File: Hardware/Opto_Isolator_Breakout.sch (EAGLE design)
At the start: 16 parts, among them Q1 NPN, Q2 NPN, U1 OPTOISOLATOR-2SOIC8

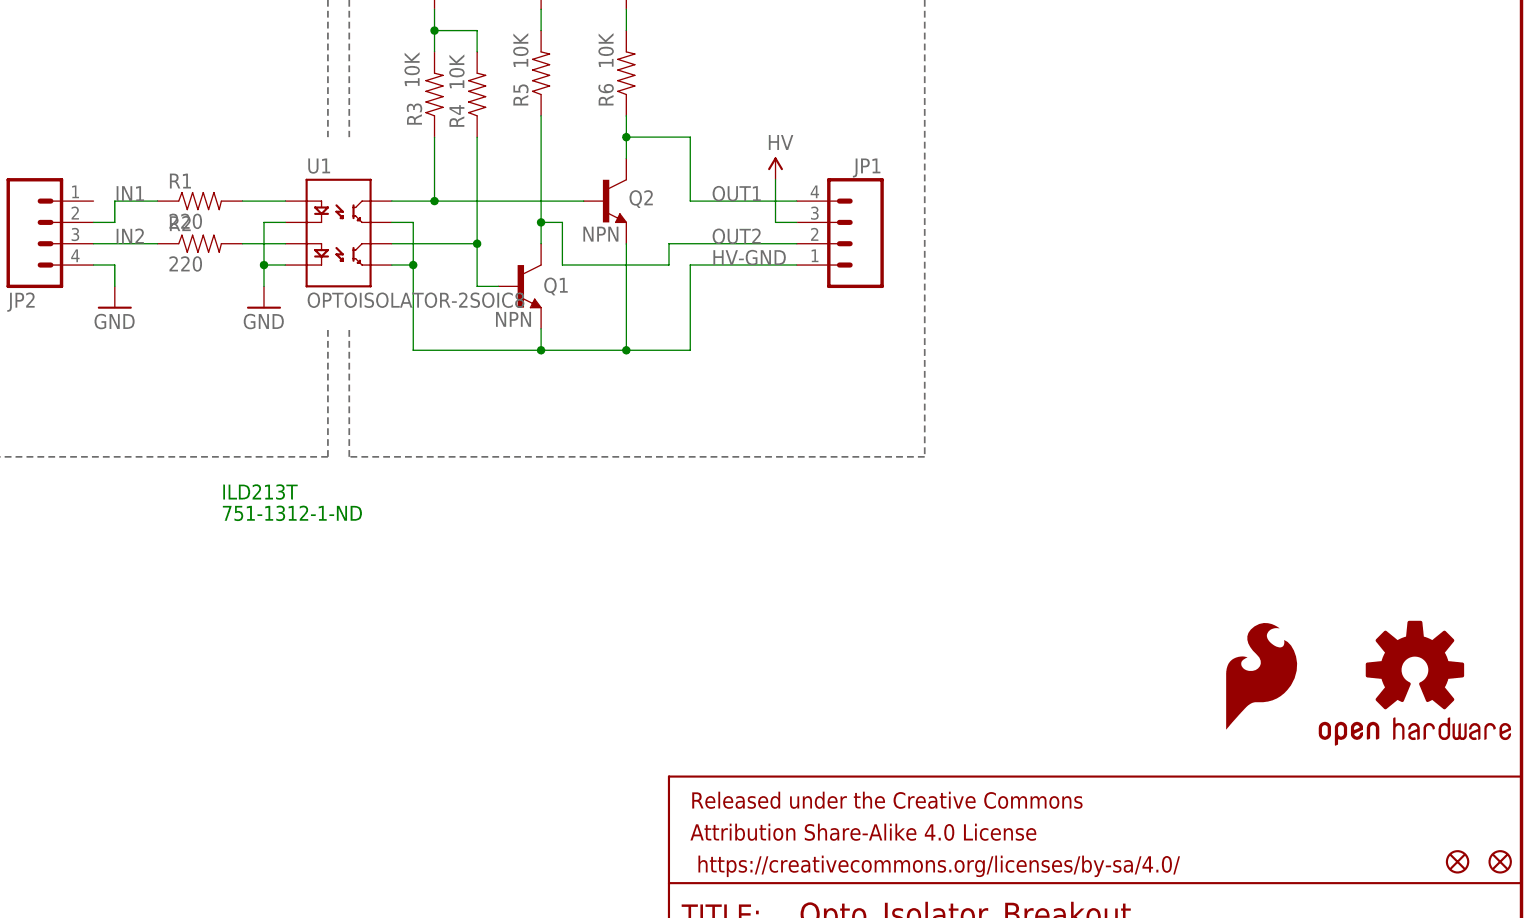
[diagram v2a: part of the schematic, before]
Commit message: Fixed qc checklist issues.
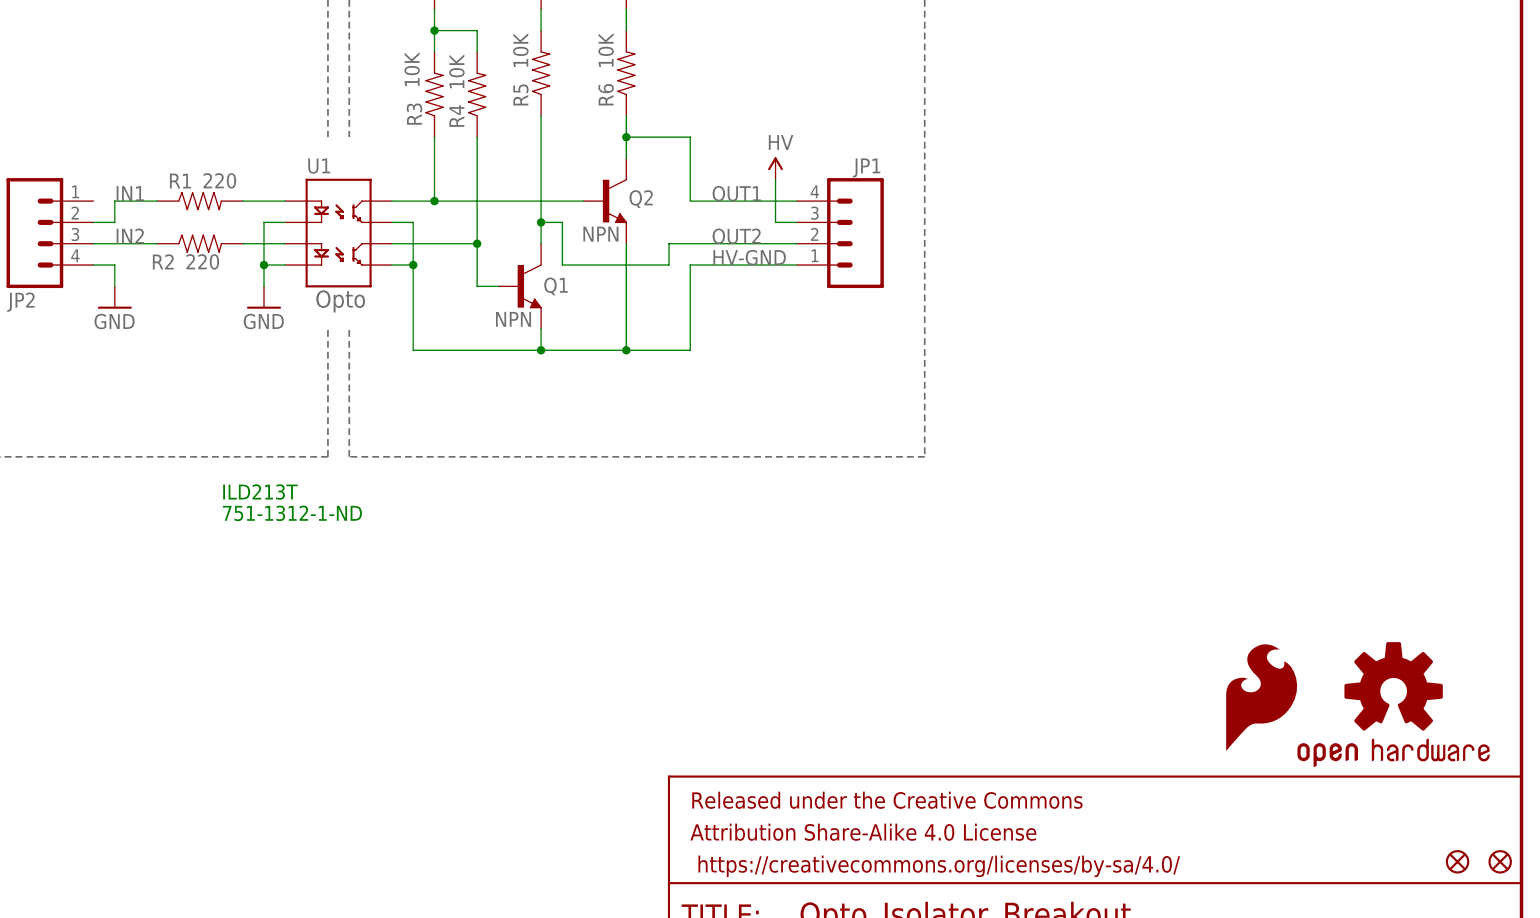
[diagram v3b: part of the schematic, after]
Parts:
- FRAME1: value FRAME-LETTER -> (none)
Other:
- note added: "Opto"
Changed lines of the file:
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@@
 <layer number="56" name="wert" color="7" fill="1" visible="no" active="no"/>
 <layer number="57" name="tCAD" color="7" fill="1" visible="no" active="no"/>
+<layer number="59" name="tCarbon" color="7" fill="1" visible="no" active="no"/>
+<layer number="60" name="bCarbon" color="7" fill="1" visible="no" active="no"/>
 <layer number="90" name="Modules" color="5" fill="1" visible="yes" active="yes"/>
 <layer number="91" name="Nets" color="2" fill="1" visible="yes" active="yes"/>
@@
 <layer number="127" name="_tValues" color="7" fill="1" visible="yes" active="yes"/>
 <layer number="128" name="_bValues" color="7" fill="1" visible="yes" active="yes"/>
+<layer number="129" name="Mask" color="7" fill="1" visible="yes" active="yes"/>
 <layer number="131" name="tAdjust" color="7" fill="1" visible="yes" active="yes"/>
 <layer number="132" name="bAdjust" color="7" fill="1" visible="yes" active="yes"/>
@@
 <layer number="251" name="SMDround" color="12" fill="11" visible="no" active="no"/>
 <layer number="254" name="cooling" color="7" fill="1" visible="yes" active="yes"/>
+<layer number="255" name="routoute" color="7" fill="1" visible="yes" active="yes"/>
 </layers>
 <schematic xreflabel="%F%N/%S" xrefpart="/%S.%C%R">
@@
 <part name="U$2" library="SparkFun-Aesthetics" deviceset="FIDUCIAL" device="UFIDUCIAL"/>
 <part name="U$3" library="SparkFun-Aesthetics" deviceset="FIDUCIAL" device="UFIDUCIAL"/>
-<part name="LOGO1" library="SparkFun-Aesthetics" deviceset="OSHW-LOGO" device="S"/>
-<part name="LOGO2" library="SparkFun-Aesthetics" deviceset="SFE_LOGO_FLAME" device=".1_INCH"/>
 <part name="R1" library="SparkFun-Resistors" deviceset="220OHM-1/10W-1%(0603)" device="" value="220"/>
 <part name="R2" library="SparkFun-Resistors" deviceset="220OHM-1/10W-1%(0603)" device="" value="220"/>
+<part name="LOGO2" library="SparkFun-Aesthetics" deviceset="SFE_LOGO_FLAME" device=".1_INCH"/>
+<part name="LOGO1" library="SparkFun-Aesthetics" deviceset="OSHW-LOGO" device="S"/>
 </parts>
 <sheets>
@@
 <text x="148.336" y="6.858" size="2.54" layer="94">Revised by: Patrick Alberts</text>
 <text x="170.434" y="11.176" size="2.54" layer="94">N.Seidle</text>
+<text x="105.156" y="91.44" size="2.032" layer="95" font="vector">Opto</text>
 </plain>
 <instances>
 <instance part="FRAME1" gate="G$1" x="0" y="0"/>
-<instance part="FRAME1" gate="G$2" x="147.32" y="0"/>
-<instance part="U1" gate="G$1" x="109.22" y="99.06"/>
+<instance part="FRAME1" gate="V" x="147.32" y="0"/>
+<instance part="U1" gate="G$1" x="109.22" y="99.06" smashed="yes">
+<attribute name="NAME" x="104.14" y="107.442" size="1.778" layer="95"/>
+</instance>
 <instance part="R3" gate="G$1" x="119.38" y="116.84" smashed="yes" rot="R90">
 <attribute name="NAME" x="117.8814" y="113.03" size="1.778" layer="95" rot="R90"/>
@@
 <instance part="U$2" gate="G$1" x="246.38" y="25.4"/>
 <instance part="U$3" gate="G$1" x="241.3" y="25.4"/>
-<instance part="LOGO1" gate="G$1" x="236.22" y="48.26"/>
-<instance part="LOGO2" gate="G$1" x="213.36" y="40.64"/>
-<instance part="R1" gate="G$1" x="91.44" y="104.14"/>
-<instance part="R2" gate="G$1" x="91.44" y="99.06"/>
+<instance part="R1" gate="G$1" x="91.44" y="104.14" smashed="yes">
+<attribute name="NAME" x="87.63" y="105.6386" size="1.778" layer="95"/>
+<attribute name="VALUE" x="91.694" y="105.664" size="1.778" layer="96"/>
+</instance>
+<instance part="R2" gate="G$1" x="91.44" y="99.06" smashed="yes">
+<attribute name="NAME" x="85.598" y="95.9866" size="1.778" layer="95"/>
+<attribute name="VALUE" x="89.662" y="96.012" size="1.778" layer="96"/>
+</instance>
+<instance part="LOGO2" gate="G$1" x="213.36" y="38.1"/>
+<instance part="LOGO1" gate="G$1" x="233.68" y="45.72"/>
 </instances>
 <busses>

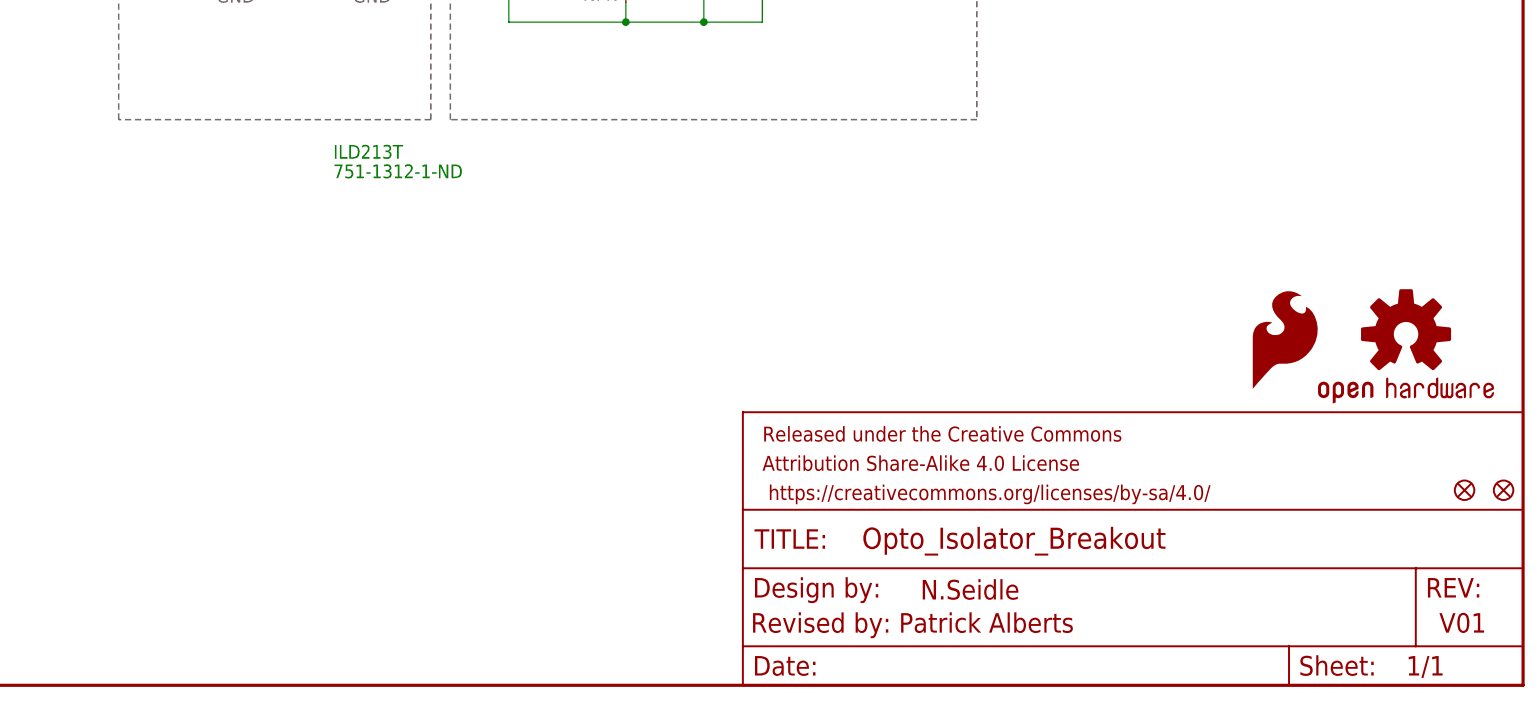
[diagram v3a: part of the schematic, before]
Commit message: Fixed final qc checklist items.
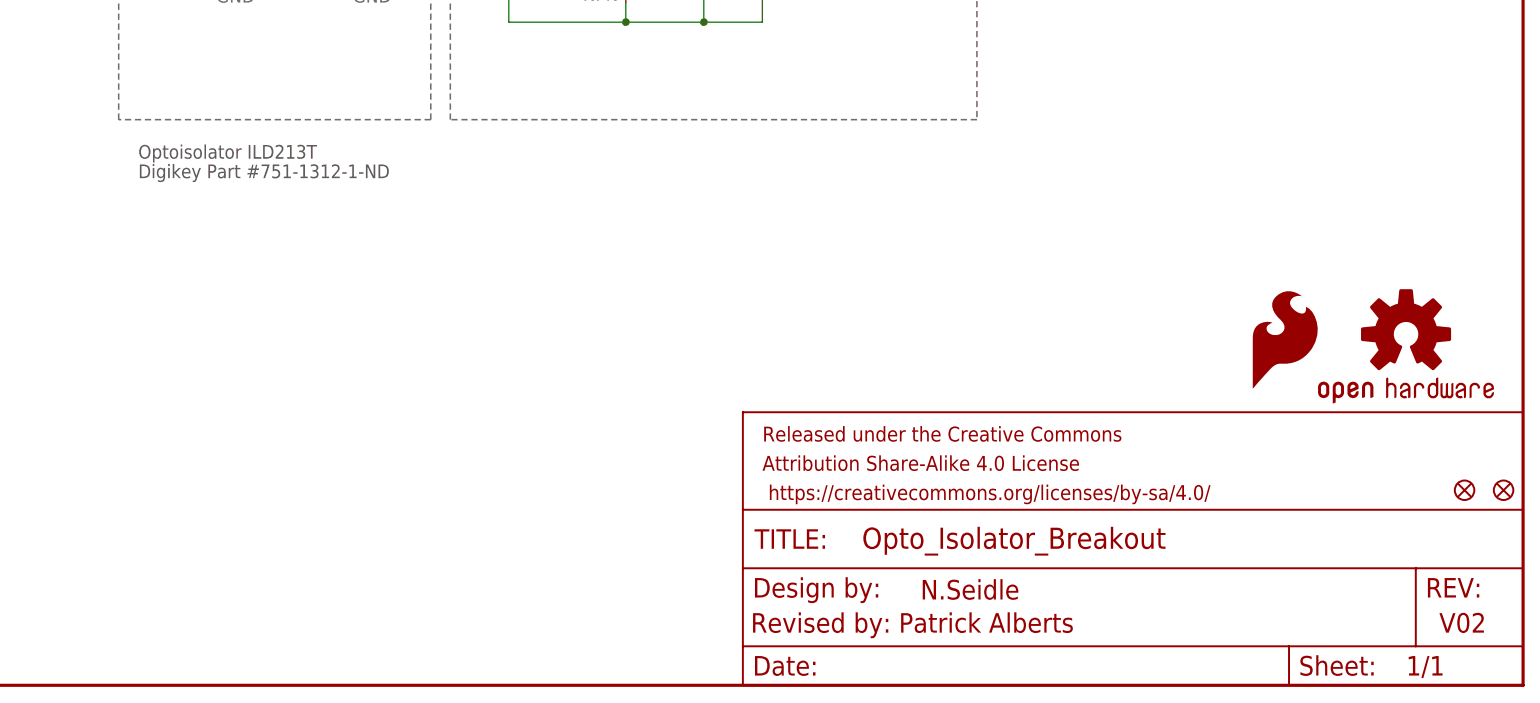
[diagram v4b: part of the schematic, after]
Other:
- note added: "Digikey Part #751-1312-1-ND"
- note added: "Optoisolator ILD213T"
- note added: "V02"
- note removed: "751-1312-1-ND"
- note removed: "ILD213T"
- note removed: "V01"
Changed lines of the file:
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@@
 <?xml version="1.0" encoding="utf-8"?>
 <!DOCTYPE eagle SYSTEM "eagle.dtd">
-<eagle version="7.1.0">
+<eagle version="6.4">
 <drawing>
 <settings>
@@
 <wire x1="177.8" y1="73.66" x2="109.22" y2="73.66" width="0.2032" layer="95" style="shortdash"/>
 <wire x1="109.22" y1="73.66" x2="109.22" y2="88.9" width="0.2032" layer="95" style="shortdash"/>
-<text x="93.98" y="68.58" size="1.778" layer="91">ILD213T</text>
-<text x="93.98" y="66.04" size="1.778" layer="91">751-1312-1-ND</text>
+<text x="68.58" y="68.58" size="1.778" layer="97">Optoisolator ILD213T</text>
+<text x="68.58" y="66.04" size="1.778" layer="97">Digikey Part #751-1312-1-ND</text>
 <text x="66.04" y="137.16" size="1.778" layer="95">3V to 5V System</text>
 <text x="157.48" y="137.16" size="1.778" layer="95">Noisy System</text>
-<text x="237.998" y="6.858" size="2.54" layer="94">V01</text>
+<text x="237.998" y="6.858" size="2.54" layer="94">V02</text>
 <text x="148.336" y="6.858" size="2.54" layer="94">Revised by: Patrick Alberts</text>
 <text x="170.434" y="11.176" size="2.54" layer="94">N.Seidle</text>

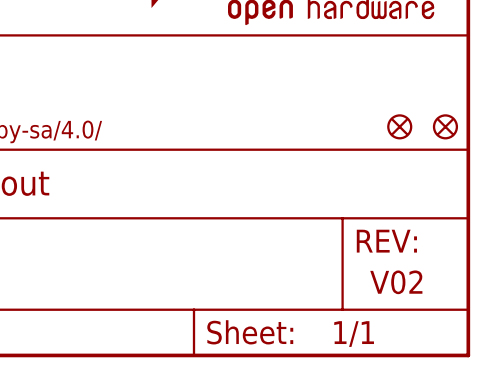
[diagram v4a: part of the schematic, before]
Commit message: Fixed QC checklist issues
Fixed version # in sch and brd
added "all units in inches" in layer 47
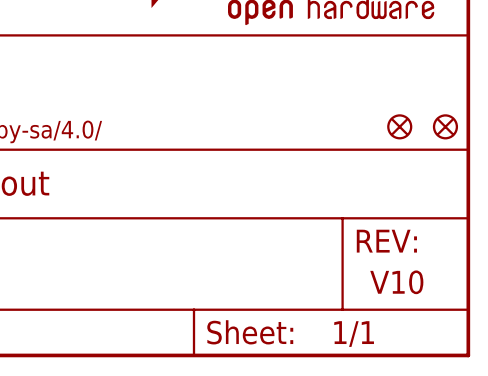
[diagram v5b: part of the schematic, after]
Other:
- note added: "V10"
- note removed: "V02"
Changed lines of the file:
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@@
 <?xml version="1.0" encoding="utf-8"?>
 <!DOCTYPE eagle SYSTEM "eagle.dtd">
-<eagle version="6.4">
+<eagle version="7.1.0">
 <drawing>
 <settings>
@@
 <text x="66.04" y="137.16" size="1.778" layer="95">3V to 5V System</text>
 <text x="157.48" y="137.16" size="1.778" layer="95">Noisy System</text>
-<text x="237.998" y="6.858" size="2.54" layer="94">V02</text>
+<text x="237.998" y="6.858" size="2.54" layer="94">V10</text>
 <text x="148.336" y="6.858" size="2.54" layer="94">Revised by: Patrick Alberts</text>
 <text x="170.434" y="11.176" size="2.54" layer="94">N.Seidle</text>
